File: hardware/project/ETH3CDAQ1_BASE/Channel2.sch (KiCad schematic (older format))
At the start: 2 parts, among them J501 Conn_02x10_Odd_Even, J502 Conn_02x10_Odd_Even

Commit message: PCB layout
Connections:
- net labels added: +18V, +18VF, -18V, -18VF
- net labels removed: +15V, +15VF, -15V, -15VF
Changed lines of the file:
@@
 Comment4 ""
 $EndDescr
-$Comp
-L ETH3CDAQ1:-15VF #PWR?
-U 1 1 602B9FBA
-P 4200 4100
-AR Path="/601F1EBA/602B9FBA" Ref="#PWR?"  Part="1"
-AR Path="/602A05D8/602B9FBA" Ref="#PWR0507"  Part="1"
-F 0 "#PWR0507" H 4200 3950 50  0001 C CNN
-F 1 "-15VF" V 4215 4227 50  0000 L CNN
-F 2 "" H 4200 4100 50  0001 C CNN
-F 3 "" H 4200 4100 50  0001 C CNN
-	1    4200 4100
-	0    -1   -1   0
-$EndComp
-$Comp
-L ETH3CDAQ1:+15VF #PWR?
-U 1 1 602B9FC0
-P 4800 4100
-AR Path="/601F1EBA/602B9FC0" Ref="#PWR?"  Part="1"
-AR Path="/602A05D8/602B9FC0" Ref="#PWR0512"  Part="1"
-F 0 "#PWR0512" H 4800 3950 50  0001 C CNN
-F 1 "+15VF" V 4815 4228 50  0000 L CNN
-F 2 "" H 4800 4100 50  0001 C CNN
-F 3 "" H 4800 4100 50  0001 C CNN
-	1    4800 4100
-	0    1    1    0
-$EndComp
 Wire Wire Line
 	4800 4100 4750 4100
@@
 Wire Wire Line
 	7250 4000 7300 4000
-$Comp
-L power:+15V #PWR?
-U 1 1 602BA056
-P 7300 4100
-AR Path="/601F1EBA/602BA056" Ref="#PWR?"  Part="1"
-AR Path="/602A05D8/602BA056" Ref="#PWR0524"  Part="1"
-F 0 "#PWR0524" H 7300 3950 50  0001 C CNN
-F 1 "+15V" V 7315 4228 50  0000 L CNN
-F 2 "" H 7300 4100 50  0001 C CNN
-F 3 "" H 7300 4100 50  0001 C CNN
-	1    7300 4100
-	0    1    1    0
-$EndComp
-$Comp
-L power:-15V #PWR?
-U 1 1 602BA05C
-P 6700 4100
-AR Path="/601F1EBA/602BA05C" Ref="#PWR?"  Part="1"
-AR Path="/602A05D8/602BA05C" Ref="#PWR0519"  Part="1"
-F 0 "#PWR0519" H 6700 4200 50  0001 C CNN
-F 1 "-15V" V 6715 4228 50  0000 L CNN
-F 2 "" H 6700 4100 50  0001 C CNN
-F 3 "" H 6700 4100 50  0001 C CNN
-	1    6700 4100
-	0    -1   -1   0
-$EndComp
 Wire Wire Line
 	4250 3700 3550 3700
@@
 Text Label 7950 3500 2    50   ~ 0
 SIGN1
+$Comp
+L ETH3CDAQ1:-18VF #PWR0507
+U 1 1 5FB6F119
+P 4200 4100
+F 0 "#PWR0507" H 4200 3950 50  0001 C CNN
+F 1 "-18VF" V 4200 4250 50  0000 L CNN
+F 2 "" H 4200 4100 50  0001 C CNN
+F 3 "" H 4200 4100 50  0001 C CNN
+	1    4200 4100
+	0    -1   -1   0
+$EndComp
+$Comp
+L ETH3CDAQ1:+18VF #PWR0512
+U 1 1 5FB6FD87
+P 4800 4100
+F 0 "#PWR0512" H 4800 3950 50  0001 C CNN
+F 1 "+18VF" V 4800 4250 50  0000 L CNN
+F 2 "" H 4800 4100 50  0001 C CNN
+F 3 "" H 4800 4100 50  0001 C CNN
+	1    4800 4100
+	0    1    1    0
+$EndComp
+$Comp
+L ETH3CDAQ1:+18V #PWR0103
+U 1 1 600291B2
+P 7300 4100
+F 0 "#PWR0103" H 7300 3950 50  0001 C CNN
+F 1 "+18V" V 7300 4250 50  0000 L CNN
+F 2 "" H 7300 4100 50  0001 C CNN
+F 3 "" H 7300 4100 50  0001 C CNN
+	1    7300 4100
+	0    1    1    0
+$EndComp
+$Comp
+L ETH3CDAQ1:-18V #PWR0104
+U 1 1 60029BC6
+P 6700 4100
+F 0 "#PWR0104" H 6700 3950 50  0001 C CNN
+F 1 "-18V" V 6700 4250 50  0000 L CNN
+F 2 "" H 6700 4100 50  0001 C CNN
+F 3 "" H 6700 4100 50  0001 C CNN
+	1    6700 4100
+	0    -1   -1   0
+$EndComp
 $EndSCHEMATC

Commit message: PCB layout
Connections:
- net +3V3: no longer J502.1 (Pin_1), J502.3 (Pin_3)
- net GND: now also J502.1 (Pin_1), J502.3 (Pin_3)
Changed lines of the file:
@@
 Wire Wire Line
 	4800 3900 4750 3900
-$Comp
-L power:+3.3V #PWR?
-U 1 1 602BA047
-P 6700 3300
-AR Path="/601F1EBA/602BA047" Ref="#PWR?"  Part="1"
-AR Path="/602A05D8/602BA047" Ref="#PWR0514"  Part="1"
-F 0 "#PWR0514" H 6700 3150 50  0001 C CNN
-F 1 "+3.3V" V 6700 3450 50  0000 L CNN
-F 2 "" H 6700 3300 50  0001 C CNN
-F 3 "" H 6700 3300 50  0001 C CNN
-	1    6700 3300
-	0    -1   -1   0
-$EndComp
-$Comp
-L power:+3.3V #PWR?
-U 1 1 602BA04D
-P 6700 3200
-AR Path="/601F1EBA/602BA04D" Ref="#PWR?"  Part="1"
-AR Path="/602A05D8/602BA04D" Ref="#PWR0513"  Part="1"
-F 0 "#PWR0513" H 6700 3050 50  0001 C CNN
-F 1 "+3.3V" V 6700 3350 50  0000 L CNN
-F 2 "" H 6700 3200 50  0001 C CNN
-F 3 "" H 6700 3200 50  0001 C CNN
-	1    6700 3200
-	0    -1   -1   0
-$EndComp
 Wire Wire Line
 	6700 3900 6750 3900
@@
 	0    -1   -1   0
 $EndComp
+$Comp
+L power:GND #PWR?
+U 1 1 5FCDC062
+P 6700 3300
+AR Path="/601F1EBA/5FCDC062" Ref="#PWR?"  Part="1"
+AR Path="/602A05D8/5FCDC062" Ref="#PWR?"  Part="1"
+F 0 "#PWR?" H 6700 3050 50  0001 C CNN
+F 1 "GND" V 6705 3172 50  0000 R CNN
+F 2 "" H 6700 3300 50  0001 C CNN
+F 3 "" H 6700 3300 50  0001 C CNN
+	1    6700 3300
+	0    1    1    0
+$EndComp
+$Comp
+L power:GND #PWR?
+U 1 1 5FCDC37C
+P 6700 3200
+AR Path="/601F1EBA/5FCDC37C" Ref="#PWR?"  Part="1"
+AR Path="/602A05D8/5FCDC37C" Ref="#PWR?"  Part="1"
+F 0 "#PWR?" H 6700 2950 50  0001 C CNN
+F 1 "GND" V 6705 3072 50  0000 R CNN
+F 2 "" H 6700 3200 50  0001 C CNN
+F 3 "" H 6700 3200 50  0001 C CNN
+	1    6700 3200
+	0    1    1    0
+$EndComp
 $EndSCHEMATC

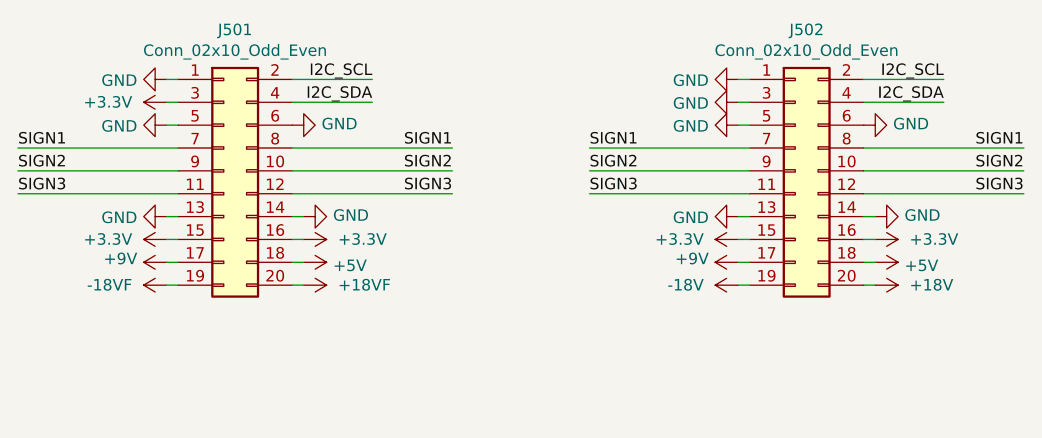
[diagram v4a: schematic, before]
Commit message: Voltage front-end development
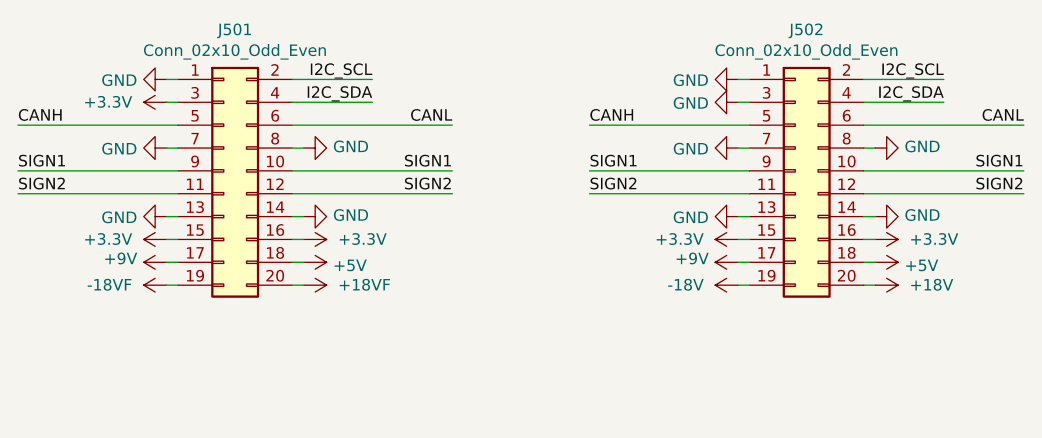
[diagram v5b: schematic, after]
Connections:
- net SIGN3 is gone; now on net SIGN2: J501.11 (Pin_11), J501.12 (Pin_12), J502.11 (Pin_11), J502.12 (Pin_12)
- net GND: now also J501.7 (Pin_7), J501.8 (Pin_8), J502.7 (Pin_7), J502.8 (Pin_8); no longer J501.5 (Pin_5), J501.6 (Pin_6), J502.5 (Pin_5), J502.6 (Pin_6)
- net SIGN1: now also J501.10 (Pin_10), J501.9 (Pin_9), J502.10 (Pin_10), J502.9 (Pin_9); no longer J501.7 (Pin_7), J501.8 (Pin_8), J502.7 (Pin_7), J502.8 (Pin_8)
- net SIGN2: no longer J501.10 (Pin_10), J501.9 (Pin_9), J502.10 (Pin_10), J502.9 (Pin_9)
- new net CANH: J501.5 (Pin_5), J502.5 (Pin_5)
- new net CANL: J501.6 (Pin_6), J502.6 (Pin_6)
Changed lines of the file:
@@
-	0    1    1    0
-$EndComp
-$Comp
-L power:GND #PWR?
-U 1 1 602B9FF8
-P 4200 3400
-AR Path="/601F1EBA/602B9FF8" Ref="#PWR?"  Part="1"
-AR Path="/602A05D8/602B9FF8" Ref="#PWR0503"  Part="1"
-F 0 "#PWR0503" H 4200 3150 50  0001 C CNN
-F 1 "GND" V 4205 3272 50  0000 R CNN
-F 2 "" H 4200 3400 50  0001 C CNN
-F 3 "" H 4200 3400 50  0001 C CNN
-	1    4200 3400
 	0    1    1    0
 $EndComp
@@
 	4250 3600 3550 3600
 Text Label 3550 3600 0    50   ~ 0
-SIGN2
+SIGN1
 Wire Wire Line
 	7250 3200 7600 3200
@@
 	4800 3800 4750 3800
 Wire Wire Line
-	4250 3400 4200 3400
-Wire Wire Line
 	4200 3300 4250 3300
 Wire Wire Line
@@
 Wire Wire Line
 	6750 3300 6700 3300
-Wire Wire Line
-	6700 3400 6750 3400
 $Comp
 L power:+3.3V #PWR?
@@
 	4250 3700 3550 3700
 Text Label 3550 3700 0    50   ~ 0
-SIGN3
+SIGN2
 Wire Wire Line
 	6700 3800 6750 3800
@@
 	7250 3800 7300 3800
 Wire Wire Line
-	4250 3500 3550 3500
-Text Label 3550 3500 0    50   ~ 0
-SIGN1
-$Comp
-L power:GND #PWR?
-U 1 1 602BA068
-P 4750 3400
-AR Path="/601F1EBA/602BA068" Ref="#PWR?"  Part="1"
-AR Path="/602A05D8/602BA068" Ref="#PWR0508"  Part="1"
-F 0 "#PWR0508" H 4750 3150 50  0001 C CNN
-F 1 "GND" V 4755 3272 50  0000 R CNN
-F 2 "" H 4750 3400 50  0001 C CNN
-F 3 "" H 4750 3400 50  0001 C CNN
-	1    4750 3400
-	0    -1   -1   0
-$EndComp
-$Comp
-L power:GND #PWR?
-U 1 1 602BA06E
-P 6700 3400
-AR Path="/601F1EBA/602BA06E" Ref="#PWR?"  Part="1"
-AR Path="/602A05D8/602BA06E" Ref="#PWR0515"  Part="1"
-F 0 "#PWR0515" H 6700 3150 50  0001 C CNN
-F 1 "GND" V 6705 3272 50  0000 R CNN
-F 2 "" H 6700 3400 50  0001 C CNN
-F 3 "" H 6700 3400 50  0001 C CNN
-	1    6700 3400
-	0    1    1    0
-$EndComp
-$Comp
-L power:GND #PWR?
-U 1 1 602BA074
-P 7250 3400
-AR Path="/601F1EBA/602BA074" Ref="#PWR?"  Part="1"
-AR Path="/602A05D8/602BA074" Ref="#PWR0520"  Part="1"
-F 0 "#PWR0520" H 7250 3150 50  0001 C CNN
-F 1 "GND" V 7255 3272 50  0000 R CNN
-F 2 "" H 7250 3400 50  0001 C CNN
-F 3 "" H 7250 3400 50  0001 C CNN
-	1    7250 3400
-	0    -1   -1   0
-$EndComp
+	4250 3400 3550 3400
+Text Label 3550 3400 0    50   ~ 0
+CANH
 Wire Wire Line
 	4750 3600 5450 3600
 Text Label 5450 3600 2    50   ~ 0
-SIGN2
+SIGN1
 Wire Wire Line
 	4750 3700 5450 3700
 Text Label 5450 3700 2    50   ~ 0
-SIGN3
-Wire Wire Line
-	4750 3500 5450 3500
-Text Label 5450 3500 2    50   ~ 0
-SIGN1
+SIGN2
+Wire Wire Line
+	4750 3400 5450 3400
+Text Label 5450 3400 2    50   ~ 0
+CANL
 Wire Wire Line
 	6750 3600 6050 3600
 Text Label 6050 3600 0    50   ~ 0
-SIGN2
+SIGN1
 Wire Wire Line
 	6750 3700 6050 3700
 Text Label 6050 3700 0    50   ~ 0
-SIGN3
-Wire Wire Line
-	6750 3500 6050 3500
-Text Label 6050 3500 0    50   ~ 0
-SIGN1
+SIGN2
+Wire Wire Line
+	6750 3400 6050 3400
+Text Label 6050 3400 0    50   ~ 0
+CANH
 Wire Wire Line
 	7250 3600 7950 3600
 Text Label 7950 3600 2    50   ~ 0
-SIGN2
+SIGN1
 Wire Wire Line
 	7250 3700 7950 3700
 Text Label 7950 3700 2    50   ~ 0
-SIGN3
-Wire Wire Line
-	7250 3500 7950 3500
-Text Label 7950 3500 2    50   ~ 0
-SIGN1
+SIGN2
+Wire Wire Line
+	7250 3400 7950 3400
+Text Label 7950 3400 2    50   ~ 0
+CANL
 $Comp
 L ETH3CDAQ1:-18VF #PWR0507
@@
 	0    1    1    0
 $EndComp
+$Comp
+L power:GND #PWR?
+U 1 1 5FCFE188
+P 4200 3500
+AR Path="/601F1EBA/5FCFE188" Ref="#PWR?"  Part="1"
+AR Path="/602A05D8/5FCFE188" Ref="#PWR0503"  Part="1"
+F 0 "#PWR0503" H 4200 3250 50  0001 C CNN
+F 1 "GND" V 4205 3372 50  0000 R CNN
+F 2 "" H 4200 3500 50  0001 C CNN
+F 3 "" H 4200 3500 50  0001 C CNN
+	1    4200 3500
+	0    1    1    0
+$EndComp
+Wire Wire Line
+	4250 3500 4200 3500
+$Comp
+L power:GND #PWR?
+U 1 1 5FCFFB88
+P 4800 3500
+AR Path="/601F1EBA/5FCFFB88" Ref="#PWR?"  Part="1"
+AR Path="/602A05D8/5FCFFB88" Ref="#PWR0508"  Part="1"
+F 0 "#PWR0508" H 4800 3250 50  0001 C CNN
+F 1 "GND" V 4805 3372 50  0000 R CNN
+F 2 "" H 4800 3500 50  0001 C CNN
+F 3 "" H 4800 3500 50  0001 C CNN
+	1    4800 3500
+	0    -1   -1   0
+$EndComp
+Wire Wire Line
+	4800 3500 4750 3500
+$Comp
+L power:GND #PWR?
+U 1 1 5FD0CD7A
+P 6700 3500
+AR Path="/601F1EBA/5FD0CD7A" Ref="#PWR?"  Part="1"
+AR Path="/602A05D8/5FD0CD7A" Ref="#PWR0515"  Part="1"
+F 0 "#PWR0515" H 6700 3250 50  0001 C CNN
+F 1 "GND" V 6705 3372 50  0000 R CNN
+F 2 "" H 6700 3500 50  0001 C CNN
+F 3 "" H 6700 3500 50  0001 C CNN
+	1    6700 3500
+	0    1    1    0
+$EndComp
+Wire Wire Line
+	6700 3500 6750 3500
+$Comp
+L power:GND #PWR?
+U 1 1 5FD0F57D
+P 7300 3500
+AR Path="/601F1EBA/5FD0F57D" Ref="#PWR?"  Part="1"
+AR Path="/602A05D8/5FD0F57D" Ref="#PWR0519"  Part="1"
+F 0 "#PWR0519" H 7300 3250 50  0001 C CNN
+F 1 "GND" V 7305 3372 50  0000 R CNN
+F 2 "" H 7300 3500 50  0001 C CNN
+F 3 "" H 7300 3500 50  0001 C CNN
+	1    7300 3500
+	0    -1   -1   0
+$EndComp
+Wire Wire Line
+	7250 3500 7300 3500
 $EndSCHEMATC

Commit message: Added selftest circuit in the base PCB.
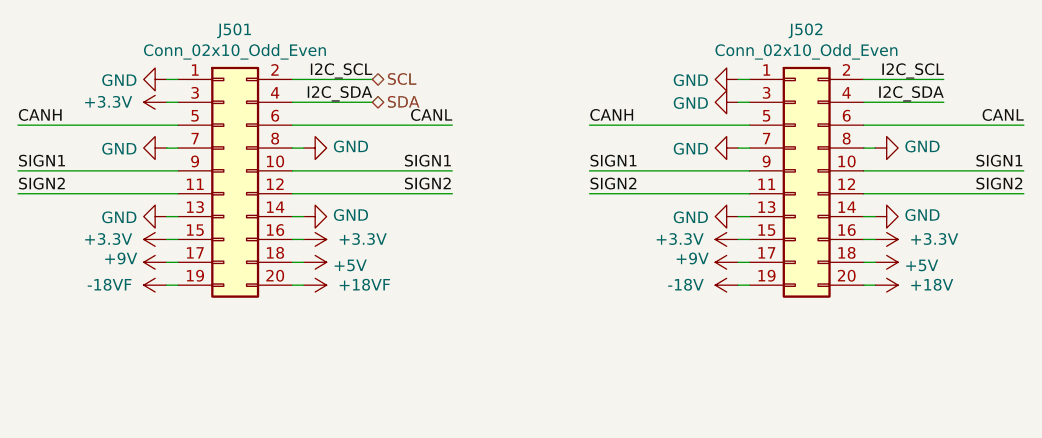
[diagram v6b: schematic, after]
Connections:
- net I2C_SCL renamed SCL
- net I2C_SDA renamed SDA
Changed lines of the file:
@@
 $Descr A4 11693 8268
 encoding utf-8
-Sheet 5 6
+Sheet 5 7
 Title ""
 Date ""
@@
 $EndComp
 $Comp
-L ETH3CDAQ1:+18V #PWR0103
+L ETH3CDAQ1:+18V #PWR0524
 U 1 1 600291B2
 P 7300 4100
-F 0 "#PWR0103" H 7300 3950 50  0001 C CNN
+F 0 "#PWR0524" H 7300 3950 50  0001 C CNN
 F 1 "+18V" V 7300 4250 50  0000 L CNN
 F 2 "" H 7300 4100 50  0001 C CNN
@@
 $EndComp
 $Comp
-L ETH3CDAQ1:-18V #PWR0104
+L ETH3CDAQ1:-18V #PWR0519
 U 1 1 60029BC6
 P 6700 4100
-F 0 "#PWR0104" H 6700 3950 50  0001 C CNN
+F 0 "#PWR0519" H 6700 3950 50  0001 C CNN
 F 1 "-18V" V 6700 4250 50  0000 L CNN
 F 2 "" H 6700 4100 50  0001 C CNN
@@
 P 7300 3500
 AR Path="/601F1EBA/5FD0F57D" Ref="#PWR?"  Part="1"
-AR Path="/602A05D8/5FD0F57D" Ref="#PWR0519"  Part="1"
-F 0 "#PWR0519" H 7300 3250 50  0001 C CNN
+AR Path="/602A05D8/5FD0F57D" Ref="#PWR0520"  Part="1"
+F 0 "#PWR0520" H 7300 3250 50  0001 C CNN
 F 1 "GND" V 7305 3372 50  0000 R CNN
 F 2 "" H 7300 3500 50  0001 C CNN
@@
 Wire Wire Line
 	7250 3500 7300 3500
+Text HLabel 5100 3200 2    50   BiDi ~ 0
+SCL
+Text HLabel 5100 3300 2    50   BiDi ~ 0
+SDA
 $EndSCHEMATC
